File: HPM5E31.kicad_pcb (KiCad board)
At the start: 4 copper layers, 75 x 50 mm, 173 parts, among them J1 Conn_ARM_JTAG_SWD_10, J10 Conn_01x06_MountingPin, J11 Conn_01x03_Pin, J12 Conn_01x04_MountingPin, J13 Conn_01x06_MountingPin, J14 USB_C_Receptacle_USB2.0_16P, J2 Conn_01x03_MountingPin, J3 RJ45_Hanrun_HR911105A_Horizon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, J4 Conn_01x04_MountingPin, J5 Conn_01x03_Pin, J6 Conn_01x02_MountingPin, J7 Conn_01x06_MountingPin, J8 Conn_01x06_MountingPin, J9 Conn_01x06_MountingPin, Q1 SS8050, Q2 SS8050, SW1 SW_Push, SW2 SW_DIP_x03, SW3 SW_DIP_x03, U1 HPM5E31IPB1, U10 REF3033, U11 RY8411, U12 XC6210B332MR, U13 AFA11-S08GLA-00, U2 LAN8720A, U3 QS-301-AGS5P, U4 MLT-5020, U6 RTL8211F-CG, U7 7*7*5-6P-L WX, U8 HR911130A, U9 USBLC6-2SC6, Y1 24Mhz, Y2 X322525MOB4SI, Y3 X322525MOB4SI

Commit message: finish
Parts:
- removed SW2, SW3: SW_DIP_x03, Button_Switch_SMD:SW_DIP_SPSTx03_Slide_KingTek_DSHP03TS_W7.62mm_P1.27mm
- added C74: 10uF, Capacitor_SMD:C_0603_1608Metric, B.Cu at (234.8, 88.1)
- added C75: 100nF, Capacitor_SMD:C_0603_1608Metric, B.Cu at (234.8, 89.5)
- added D5: ESD9B3.3ST5G, Diode_SMD:D_SOD-323, F.Cu at (234.4, 72.1)
- added D6: ESD9B3.3ST5G, Diode_SMD:D_SOD-323, F.Cu at (234.4, 75.5)
- added D7: ESD9B3.3ST5G, Diode_SMD:D_SOD-323, F.Cu at (234.4, 78.9)
- added D8: ESD9B3.3ST5G, Diode_SMD:D_SOD-323, F.Cu at (234.4, 82.5)
- added G***: LOGO, LOGO, F.Cu at (211.5, 72.9)
- added H1: MountingHole_Pad, MountingHole:MountingHole_2.2mm_M2_Pad, F.Cu at (228.8, 61.0)
- added H2: MountingHole_Pad, MountingHole:MountingHole_2.2mm_M2_Pad, F.Cu at (228.8, 106.0)
- added H3: MountingHole_Pad, MountingHole:MountingHole_2.2mm_M2_Pad, F.Cu at (185.0, 61.0)
- added H4: MountingHole_Pad, MountingHole:MountingHole_2.2mm_M2_Pad, F.Cu at (185.0, 106.0)
- added J15: Conn_01x03_Socket, Connector_Harwin:Harwin_M20-89003xx_1x03_P2.54mm_Horizontal, B.Cu at (203.8, 112.3)
- added J16: Conn_01x04_Socket, Connector_Harwin:Harwin_M20-89004xx_1x04_P2.54mm_Horizontal, B.Cu at (178.9, 68.5)
- added R55: 4.7K, Resistor_SMD:R_0603_1608Metric, F.Cu at (226.1, 87.5)
- added R56: 4.7K, Resistor_SMD:R_0603_1608Metric, F.Cu at (226.1, 88.9)
- added R57: 4.7K, Resistor_SMD:R_0603_1608Metric, F.Cu at (226.1, 90.3)
- added R58: 4.7K, Resistor_SMD:R_0603_1608Metric, F.Cu at (220.0, 68.4)
- added R59: 4.7K, Resistor_SMD:R_0603_1608Metric, F.Cu at (220.0, 69.9)
- added R60: 4.7K, Resistor_SMD:R_0603_1608Metric, F.Cu at (220.0, 71.4)
- added R61: 120R, Resistor_SMD:R_0603_1608Metric, F.Cu at (203.5, 66.1)
- added U5: TJA1051TK-3, Package_SON:HVSON-8-1EP_3x3mm_P0.65mm_EP1.6x2.4mm, F.Cu at (200.6, 66.3)
- C10, C11, C12, C13, C16, C19, C20, C21, C22, C54, C55, C56, C57, C58, C72, C73, C8, C9, Q1, Q2, R16, R17, R18, R19, R20, R21, R3, R4, R42, R43, R44, R45, R46, R47, R48, R49, R5, R50, R6: moved to B.Cu
- C25, C26, C37, C38, C39, C46, R13, R14, R15: moved to F.Cu
- J5: footprint Connector_PinHeader_2.54mm:PinHeader_1x03_P2.54mm_Horizontal -> Connector_PinHeader_2.54mm:PinHeader_1x03_P2.54mm_Vertical
- U2: footprint Package_DFN_QFN:VQFN-24-1EP_4x4mm_P0.5mm_EP2.5x2.5mm_ThermalVias -> Package_DFN_QFN:VQFN-24-1EP_4x4mm_P0.5mm_EP2.5x2.5mm
- Y1, Y2, Y3: footprint Crystal:Crystal_SMD_3225-4Pin_3.2x2.5mm -> Crystal:Crystal_SMD_2016-4Pin_2.0x1.6mm
- moved J7 69.3 mm to (185.6, 97.6), turned to -90 degrees
- moved J8 68.8 mm to (185.6, 78.0), turned to -90 degrees
- moved R50 68.6 mm to (252.4, 61.0), turned to 90 degrees
- moved J14 67.0 mm to (253.4, 63.6), turned to 90 degrees
- moved R49 64.7 mm to (252.4, 65.8), turned to -90 degrees
- moved J4 64.7 mm to (185.6, 87.8), turned to -90 degrees
- moved J12 62.3 mm to (185.6, 68.1), turned to -90 degrees
- moved J13 61.7 mm to (193.1, 61.6), turned to 180 degrees
- moved J9 60.8 mm to (193.8, 105.5), turned to 0 degrees
- moved J11 59.6 mm to (190.6, 91.2)
- moved Q2 58.6 mm to (191.9, 99.2), turned to 90 degrees
- moved J6 57.7 mm to (202.2, 61.6), turned to 180 degrees
- moved R21 57.2 mm to (189.5, 99.1)
- moved U13 56.4 mm to (191.8, 97.6)
- moved R20 54.3 mm to (194.1, 99.2), turned to -90 degrees
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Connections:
- J12 pad 1: /PIN_BCD/I2C3.SDA -> +3.3V
- J12 pad 2: /PIN_BCD/I2C3.SCL -> GND
- J12 pad 3: GND -> /PIN_BCD/I2C3.SCL
- J12 pad 4: +3.3V -> /PIN_BCD/I2C3.SDA
- J12 pad MP: +3.3V -> GND
- J4 pad 1: /PIN_BCD/UART3.RXD -> +3.3V
- J4 pad 2: /PIN_BCD/UART3.TXD -> GND
- J4 pad 3: GND -> /PIN_BCD/UART3.TXD
- J4 pad 4: +3.3V -> /PIN_BCD/UART3.RXD
- J6 pad 1: /PIN_BCD/MCAN2.RXD -> Net-(J6-Pin_1)
- J6 pad 2: /PIN_BCD/MCAN2.TXD -> Net-(J6-Pin_2)
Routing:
- net +3.3V: track 0.00 -> 345.9 mm, vias 0 -> 45
- net GND: track 0.00 -> 123.8 mm, vias 0 -> 264
- net +5V: track 0.00 -> 101.6 mm, vias 0 -> 10
- net /PIN_A/MDC: track 0.00 -> 91.0 mm, vias 0 -> 2
- net /PIN_A/MDIO: track 0.00 -> 86.6 mm, vias 0 -> 2
- net Net-(U1A-DCDC_SNS): track 0.00 -> 64.6 mm, vias 0 -> 8
- net /PIN_F/ADC1.IN10: track 0.00 -> 61.5 mm, vias 0 -> 2
- net /PIN_A/ENCODER_B: track 0.00 -> 61.0 mm, vias 0 -> 2
- net /Crystal/USB_DP: track 0.00 -> 58.4 mm, vias 0 -> 2
- net /PIN_A/ENCODER_KEY: track 0.00 -> 58.2 mm, vias 0 -> 2
- net GNDA: track 0.00 -> 58.0 mm, vias 0 -> 8
- net /Crystal/USB_DN: track 0.00 -> 58.0 mm, vias 0 -> 2
- net /PIN_F/UP: track 0.00 -> 56.2 mm, vias 0 -> 3
- net /PIN_A/EMCODER_A: track 0.00 -> 55.6 mm, vias 0 -> 2
- net /PIN_F/ADC0.IN00: track 0.00 -> 54.9 mm, vias 0 -> 2
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- added copper zone on F.Cu, net +3.3V
- added copper zone on In2.Cu, net +3.3V
- added copper zone on F.Cu, net +3.3VA
- added copper zone on F.Cu, net +5V
- added copper zone on In2.Cu, net +5V
- added copper zone on B.Cu, net GND
- added copper zone on F.Cu, net GND
- added copper zone on In1.Cu, net GND
- added copper zone on In2.Cu, net GND
- added copper zone on F.Cu, net GNDA
- added copper zone on B.Cu, net GNDPWR
- added copper zone on F.Cu, net GNDPWR
- added copper zone on In1.Cu, net GNDPWR
- added copper zone on In2.Cu, net GNDPWR
- added copper zone on F.Cu, net Net-(F1-Pad1)
- added copper zone on F.Cu, net Net-(U11-SW)
- added copper zone on F.Cu, net Net-(U1A-DCDC_SNS)
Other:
- outline, holes or cut-outs redrawn
- board text added: "3.3V"
- board text added: "3V3"
- board text added: "5V"
- board text added: "ADC0.IN0"
- board text added: "ADC0.IN1"
- board text added: "ADC0.IN2"
- board text added: "ADC0.IN3"
- board text added: "ADC1.IN10"
- board text added: "ADC1.IN8"
- board text added: "CAN2_H"
- board text added: "CAN2_L"
- board text added: "DOWN"
- board text added: "ETHERCAT"
- board text added: "ETHERNET"
- board text added: "GND"
- board text added: "IIC3"
- board text added: "JTAG"
- board text added: "LEDA"
- board text added: "PC16"
- board text added: "PWM0.P0"
- board text added: "PWM0.P1"
- board text added: "PWM0.P2"
- board text added: "PWM0.P3"
- board text added: "PWM0.P4"
- board text added: "PWM0.P5"
- board text added: "QEI1.A"
- board text added: "QEI1.B"
- board text added: "QEI1.F"
- board text added: "RIGHT"
- board text added: "RST"
- board text added: "RX"
- board text added: "SCL"
- board text added: "SDA"
- board text added: "SPI.CS0"
- board text added: "SPI.MISO"
- board text added: "SPI.MOSI"
- board text added: "SPI.SCLK"
- board text added: "TM2.CT0"
- board text added: "TX"
- board text added: "UART0"
- board text added: "UART3.RX"
- board text added: "UART3.TX"
- board text added: "UP"
- board text added: "U_phase"
- board text added: "V_phase"
- board text added: "WS2812"
- board text added: "W_phase"

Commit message: demo第一版
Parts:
- added R62: 10R, Resistor_SMD:R_0603_1608Metric, F.Cu at (219.4, 98.5)
- added R63: 4.7K, Resistor_SMD:R_0402_1005Metric, F.Cu at (219.3, 79.5)
- added R64: 4.7K, Resistor_SMD:R_0402_1005Metric, F.Cu at (219.3, 81.4)
- added R65: 4.7K, Resistor_SMD:R_0402_1005Metric, F.Cu at (219.4, 74.9)
- added TP1: TestPoint, TestPoint:TestPoint_Pad_D1.0mm, F.Cu at (221.6, 60.2)
- added TP2: TestPoint, TestPoint:TestPoint_Pad_D1.0mm, F.Cu at (225.2, 60.2)
- added TP3: TestPoint, TestPoint:TestPoint_Pad_D1.0mm, F.Cu at (223.4, 60.2)
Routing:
- net +5V: track 101.6 -> 106.2 mm, vias 10 -> 11
- net /PIN_F/VCC3V3_PHY: track 45.5 -> 48.9 mm, vias 7 -> 9
- net GND: track 123.8 -> 127.0 mm, vias 264 -> 320
- net +3.3V: track 345.9 -> 348.1 mm, vias 45 -> 46
- net /PIN_F/ETH0.RXCK: track 17.2 -> 18.4 mm
- net /PIN_F/PHYRSTB: track 40.8 -> 41.5 mm
- net /PIN_BCD/I2C3.SCL: vias 2 -> 1
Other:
- board text added: "0"
- board text added: "0/1"
- board text added: "1"
- board text added: "ADDRESS=010"
- board text added: "ADDRESS=1"
- board text added: "JLCJLCJLCJLC"
- board text added: "x"

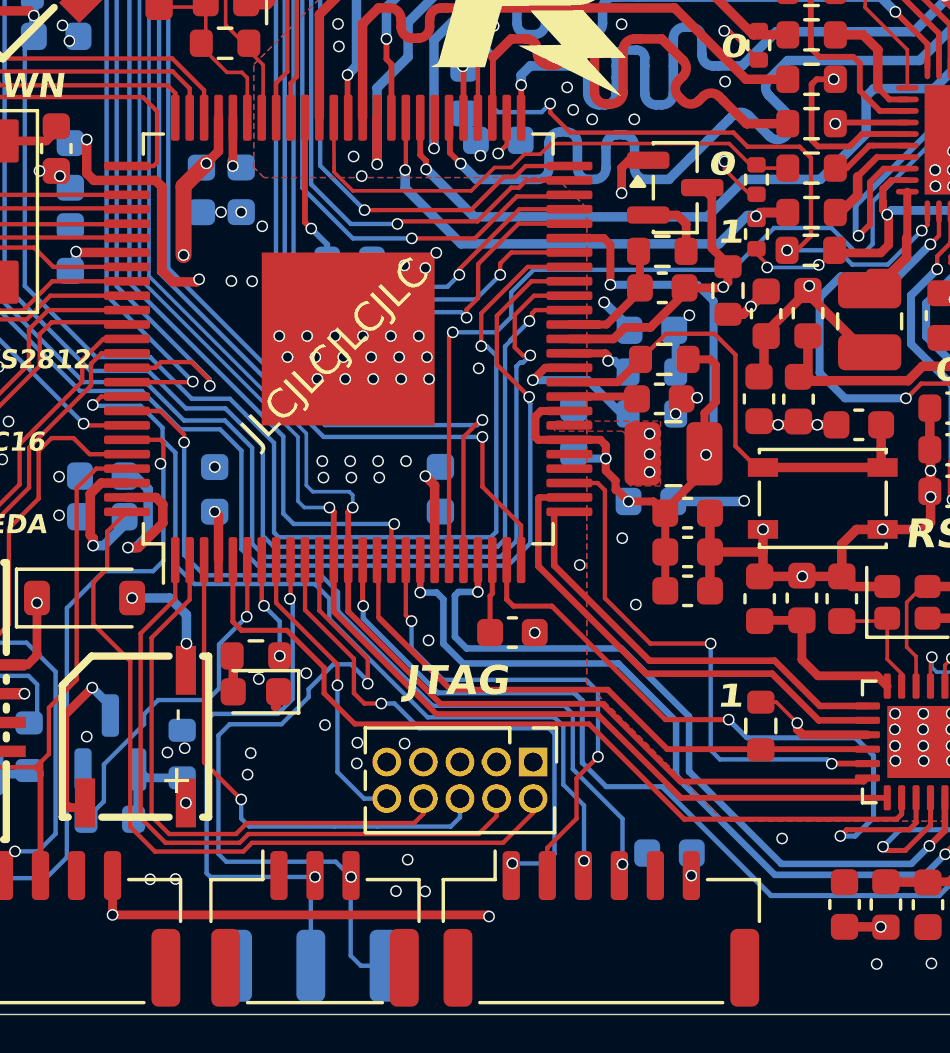
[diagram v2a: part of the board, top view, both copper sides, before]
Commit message: modify silkscreen printing
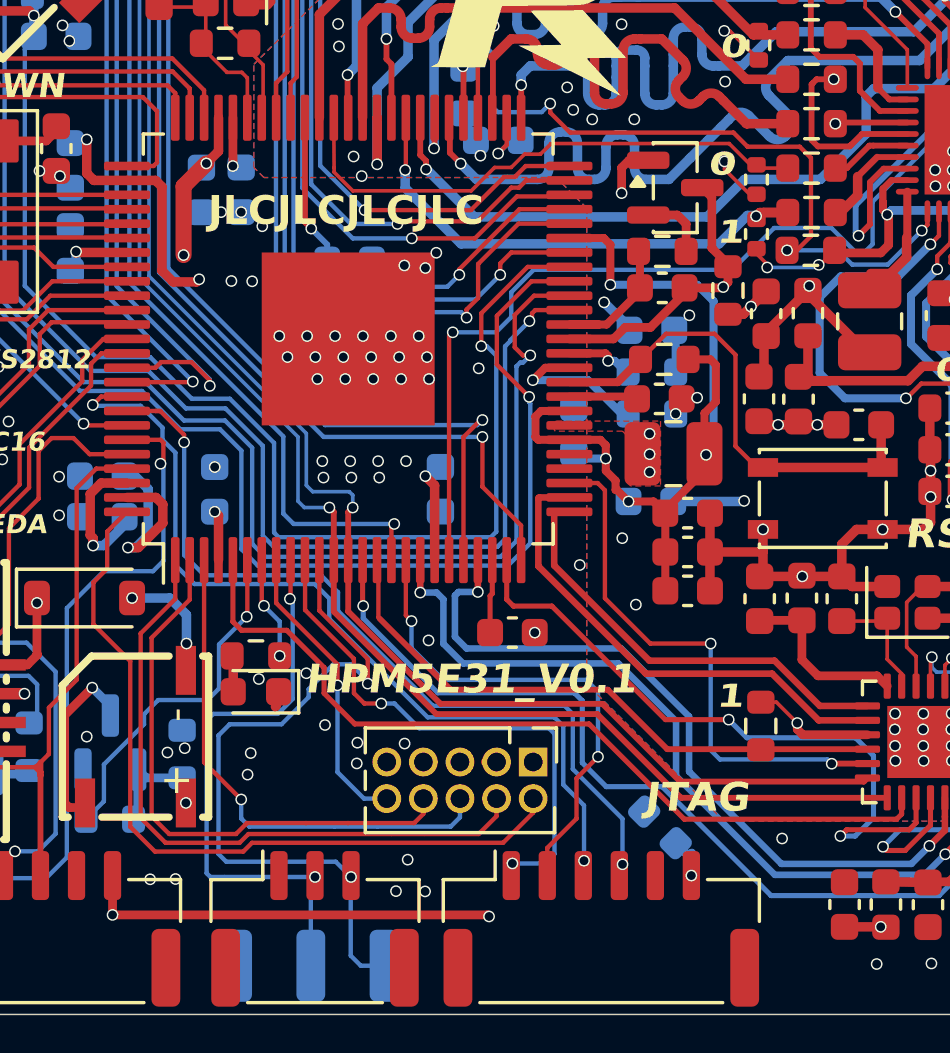
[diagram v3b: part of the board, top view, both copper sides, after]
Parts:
- moved C16 0.95 mm to (215.9, 102.0), turned to -45 degrees
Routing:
- net +3.3V: track 348.1 -> 349.1 mm
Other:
- board text added: "HPM5E31_V0.1"
